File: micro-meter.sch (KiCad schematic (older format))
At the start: 118 parts, among them U1 XC6206P332MR, U2 STM32F411CEU6

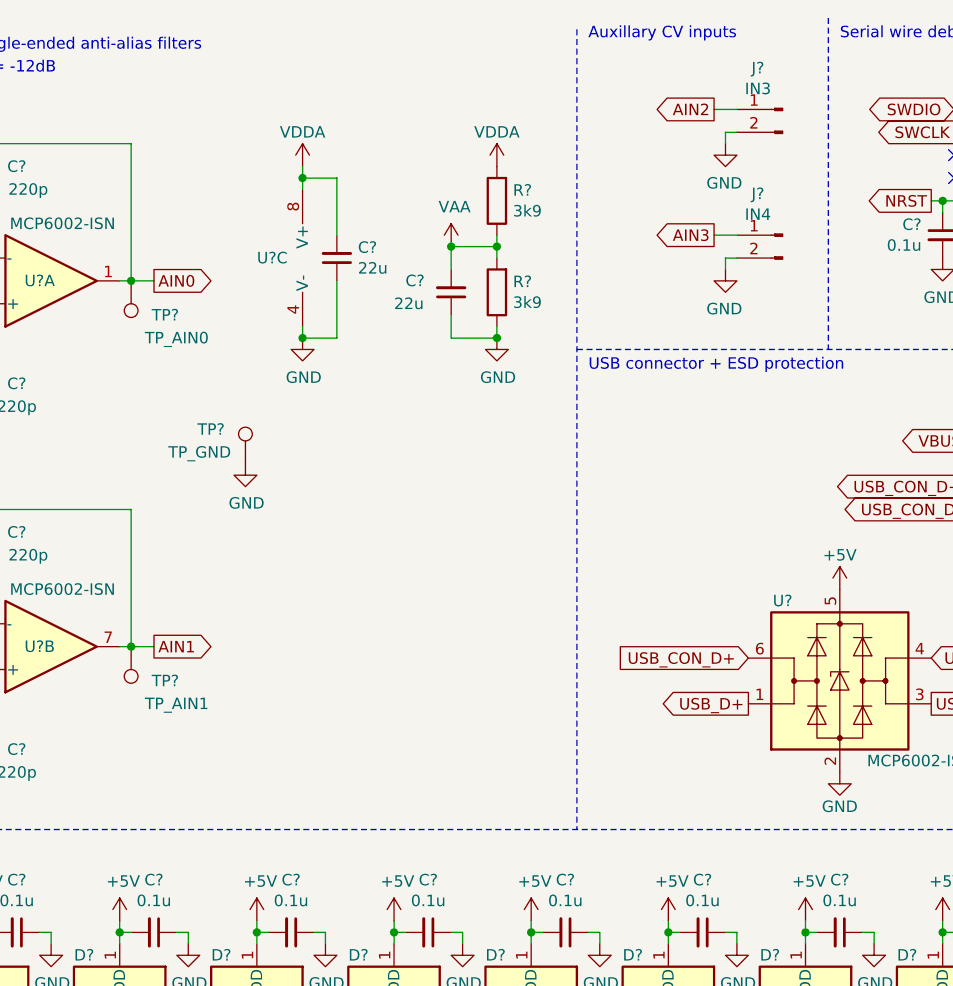
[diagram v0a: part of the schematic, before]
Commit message: Add testpoints
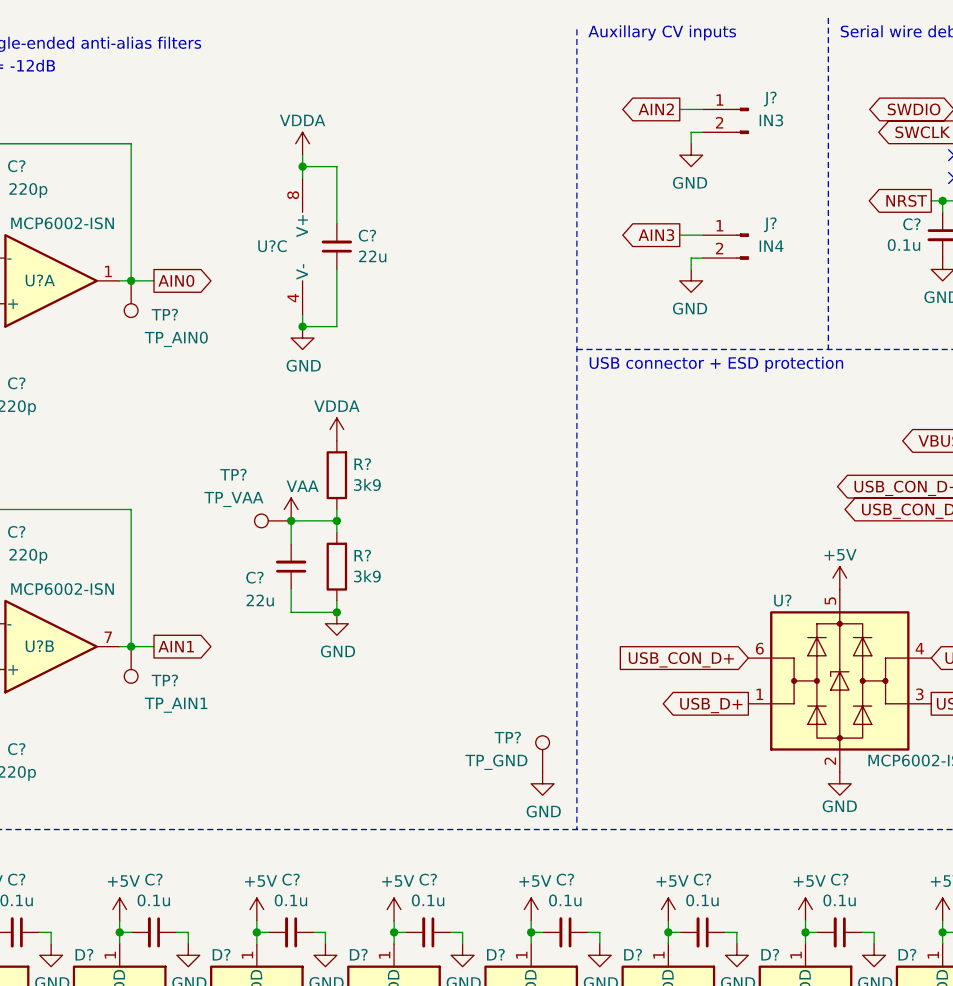
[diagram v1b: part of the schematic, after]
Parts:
- added TP?: TP_VAA, symbol Connector:TestPoint
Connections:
- net VAA: now also TP?.1
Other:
- moved on the sheet: C?, J?, R?, TP?, U?C

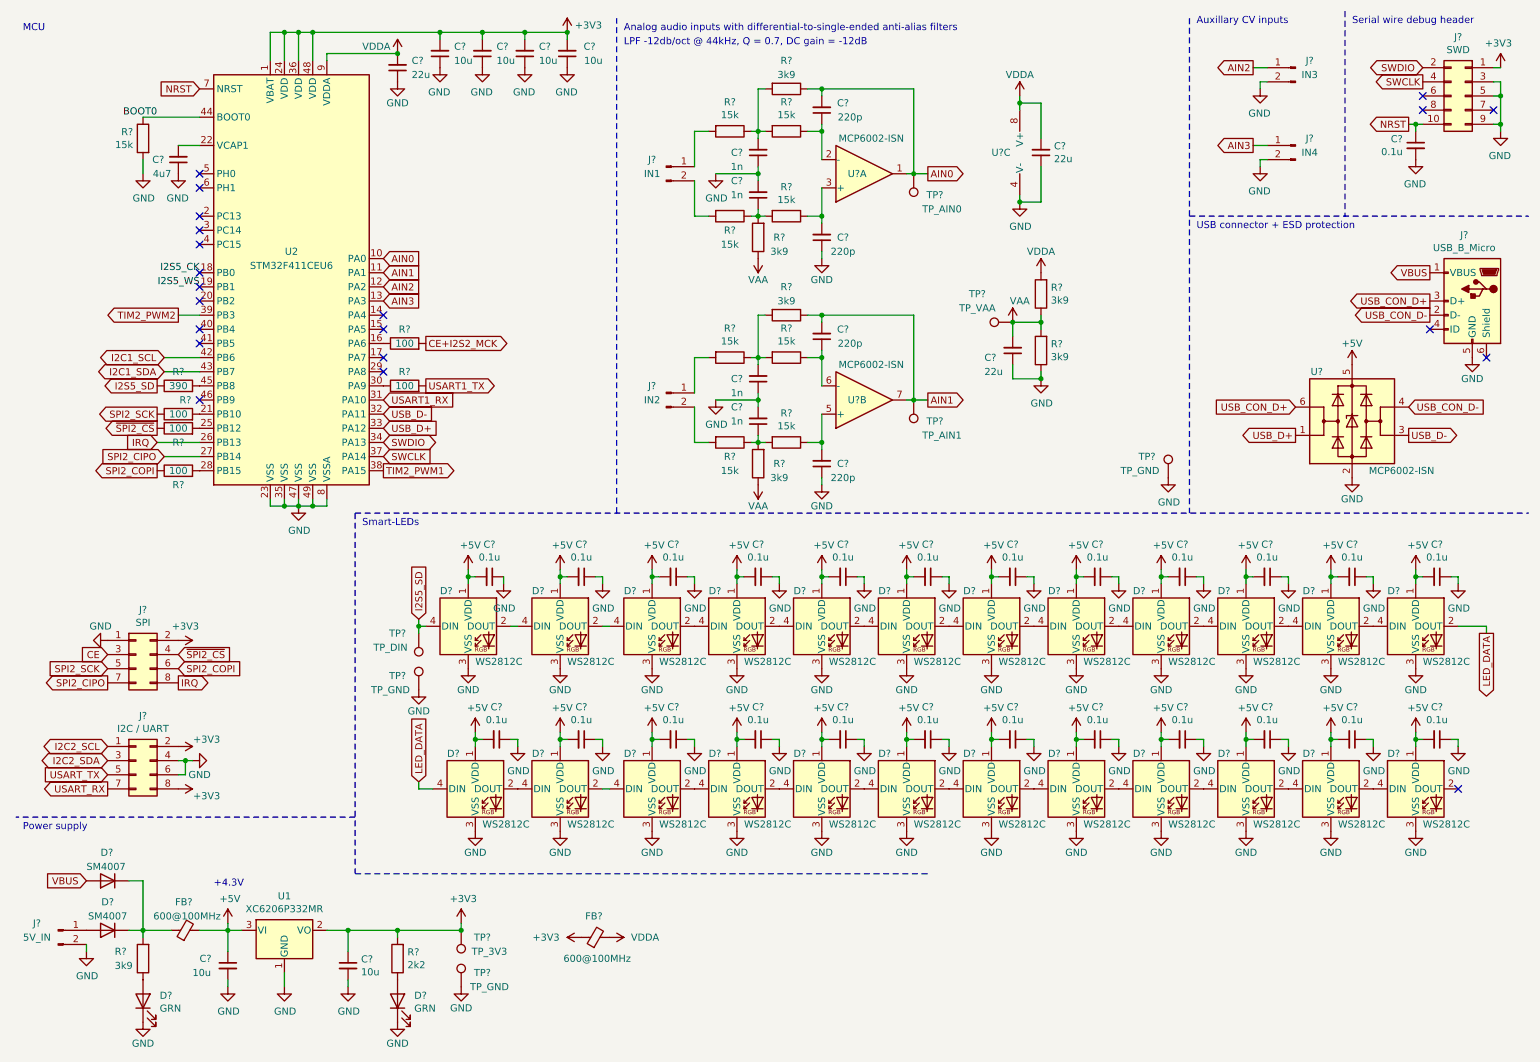
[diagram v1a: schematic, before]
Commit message: Annotate and assign footprints
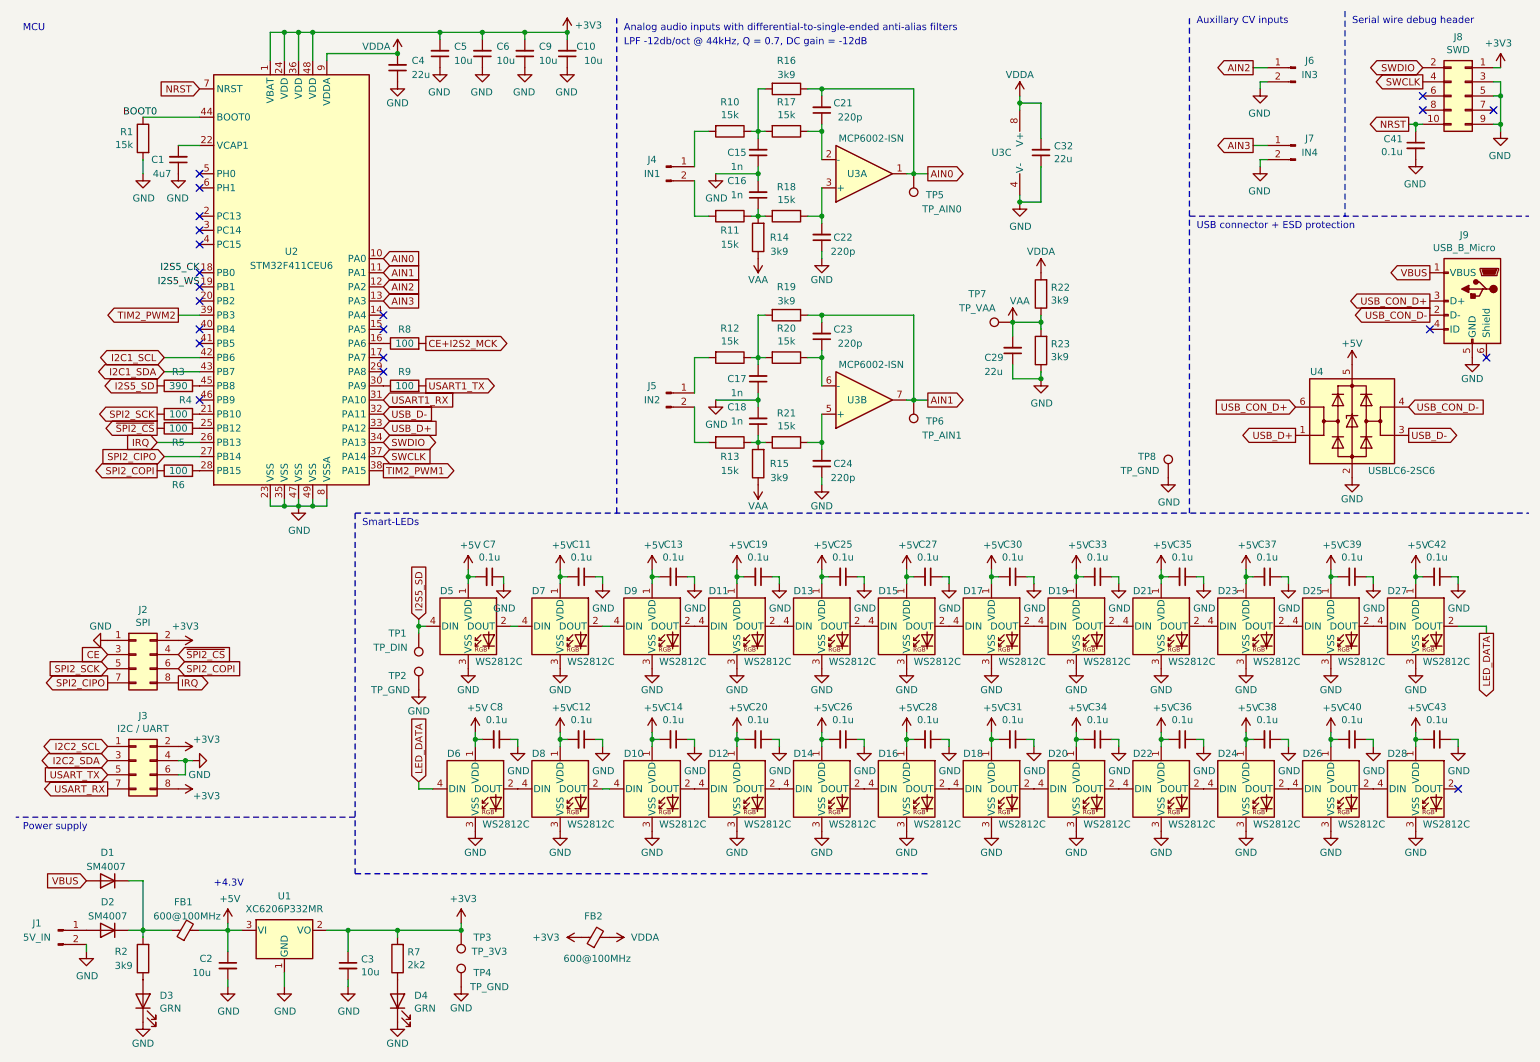
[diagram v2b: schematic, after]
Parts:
- C1, C10, C11, C12, C13, C14, C15, C16, C17, C18, C19, C2, C20, C21, C22, C23, C24, C25, C26, C27, C28, C29, C3, C30, C31, C32, C33, C34, C35, C36, C37, C38, C39, C4, C40, C41, C42, C43, C5, C6, C7, C8, C9: renamed from C?; footprint (none) -> Capacitor_SMD:C_0603_1608Metric
- D1, D2: renamed from D?; footprint Diode_SMD:D_MELF -> Diode_SMD:D_SOD-123F
- D3, D4: renamed from D?; footprint (none) -> LED_SMD:LED_0805_2012Metric
- FB1, FB2: renamed from FB?; footprint (none) -> Resistor_SMD:R_0805_2012Metric
- J1, J4, J5, J6, J7: renamed from J?; footprint (none) -> Connector_PinSocket_2.54mm:PinSocket_1x02_P2.54mm_Vertical
- J2, J3: renamed from J?; footprint (none) -> Connector_PinSocket_2.54mm:PinSocket_2x04_P2.54mm_Vertical
- J8: renamed from J?; footprint (none) -> Connector_PinHeader_1.27mm:PinHeader_2x05_P1.27mm_Vertical
- J9: renamed from J?; footprint (none) -> Connector_USB:USB_Micro-B_Amphenol_10103594-0001LF_Horizontal
- R1, R10, R11, R12, R13, R14, R15, R16, R17, R18, R19, R2, R20, R21, R22, R23, R3, R4, R5, R6, R7, R8, R9: renamed from R?; footprint (none) -> Resistor_SMD:R_0603_1608Metric
- TP1, TP3, TP5, TP6, TP7: renamed from TP?; footprint (none) -> TestPoint:TestPoint_Pad_2.0x2.0mm
- TP2, TP4, TP8: renamed from TP?; footprint (none) -> TestPoint:TestPoint_Loop_D2.50mm_Drill1.0mm
- U3: renamed from U?; footprint (none) -> Package_SO:SOIC-8_3.9x4.9mm_P1.27mm
- U4: renamed from U?; value MCP6002-ISN -> USBLC6-2SC6; footprint (none) -> Package_TO_SOT_SMD:SOT-23-6
- gave numbers to parts that had none: 24

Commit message: Add crystal and i2c pullups
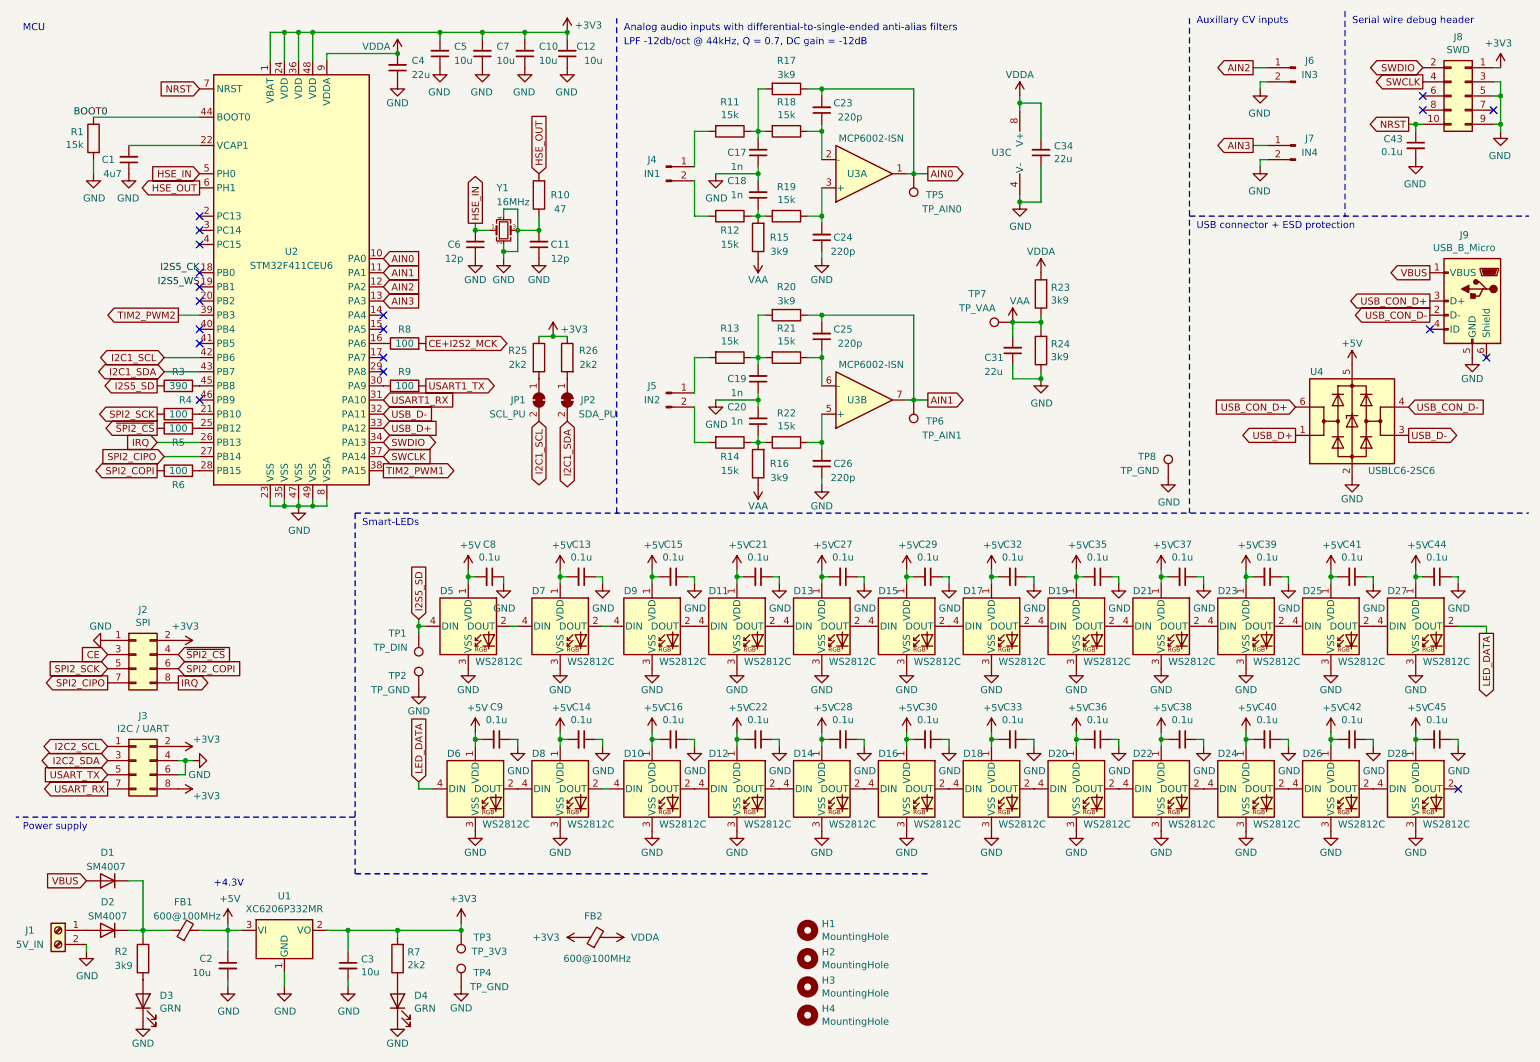
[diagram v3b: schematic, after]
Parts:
- removed J1: 5V_IN, Connector_PinSocket_2.54mm:PinSocket_1x02_P2.54mm_Vertical, symbol Connector:Conn_01x02_Male
- added C11, C6: 12p, Capacitor_SMD:C_0402_1005Metric, symbol Device:C_Small
- added H1, H2, H3, H4: MountingHole, MountingHole:MountingHole_3.2mm_M3, symbol Mechanical:MountingHole
- added J1: 5V_IN, Connector_PinSocket_2.54mm:PinSocket_1x02_P2.54mm_Vertical, symbol Connector:Screw_Terminal_01x02
- added JP1: SCL_PU, Jumper:SolderJumper-2_P1.3mm_Open_RoundedPad1.0x1.5mm, symbol Jumper:SolderJumper_2_Bridged
- added JP2: SDA_PU, Jumper:SolderJumper-2_P1.3mm_Open_RoundedPad1.0x1.5mm, symbol Jumper:SolderJumper_2_Bridged
- added R10: 47, Resistor_SMD:R_0402_1005Metric, symbol Device:R
- added R25, R26: 2k2, Resistor_SMD:R_0603_1608Metric, symbol Device:R
- added Y1: 16MHz, Crystal:Crystal_SMD_3225-4Pin_3.2x2.5mm, symbol Device:Crystal_GND24_Small
- J9: footprint Connector_USB:USB_Micro-B_Amphenol_10103594-0001LF_Horizontal -> Connector_USB:USB_Micro-B_Wuerth_629105150521
- R1: footprint Resistor_SMD:R_0603_1608Metric -> Resistor_SMD:R_0402_1005Metric
- renumbered C9 to C10, C10 to C12, C11 to C13, C12 to C14, C13 to C15, C14 to C16, C15 to C17, C16 to C18, C17 to C19, C18 to C20, C19 to C21, C20 to C22, C21 to C23, C22 to C24, C23 to C25, C24 to C26, C25 to C27, C26 to C28, C27 to C29, C28 to C30, C29 to C31, C30 to C32, C31 to C33, C32 to C34, C33 to C35, C34 to C36, C35 to C37, C36 to C38, C37 to C39, C38 to C40, C39 to C41, C40 to C42, C41 to C43, C42 to C44, C43 to C45, C6 to C7, C7 to C8, C8 to C9, R10 to R11, R11 to R12, R12 to R13, R13 to R14, R14 to R15, R15 to R16, R16 to R17, R17 to R18, R18 to R19, R19 to R20, R20 to R21, R21 to R22, R22 to R23, R23 to R24
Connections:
- net +3V3: now also R25.1, R26.1
- net GND: now also C11.1, C11.2, C6.1, J1.2 (Pin_2), R10.1, Y1.2, Y1.3, Y1.4
- net I2C1_SCL: now also JP1.2 (B)
- net I2C1_SDA: now also JP2.2 (B)
- net at D2.2 (A): now also J1.1 (Pin_1)
- net HSE_IN: now reaches U2.5 (PH0)
- net HSE_IN: now also C6.2, Y1.1
- net HSE_OUT: now reaches U2.6 (PH1)
- net HSE_OUT: now also R10.2
- new net: JP1.1 (A), R25.2
- new net: JP2.1 (A), R26.2
- no-connect marks 21 -> 19
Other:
- moved on the sheet: C1, R1
